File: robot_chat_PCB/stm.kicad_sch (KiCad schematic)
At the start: 12 parts, among them J3 Conn_02x07_Odd_Even, SW1 SW_Push, U1 STM32G070RBTx, Y1 16MHz

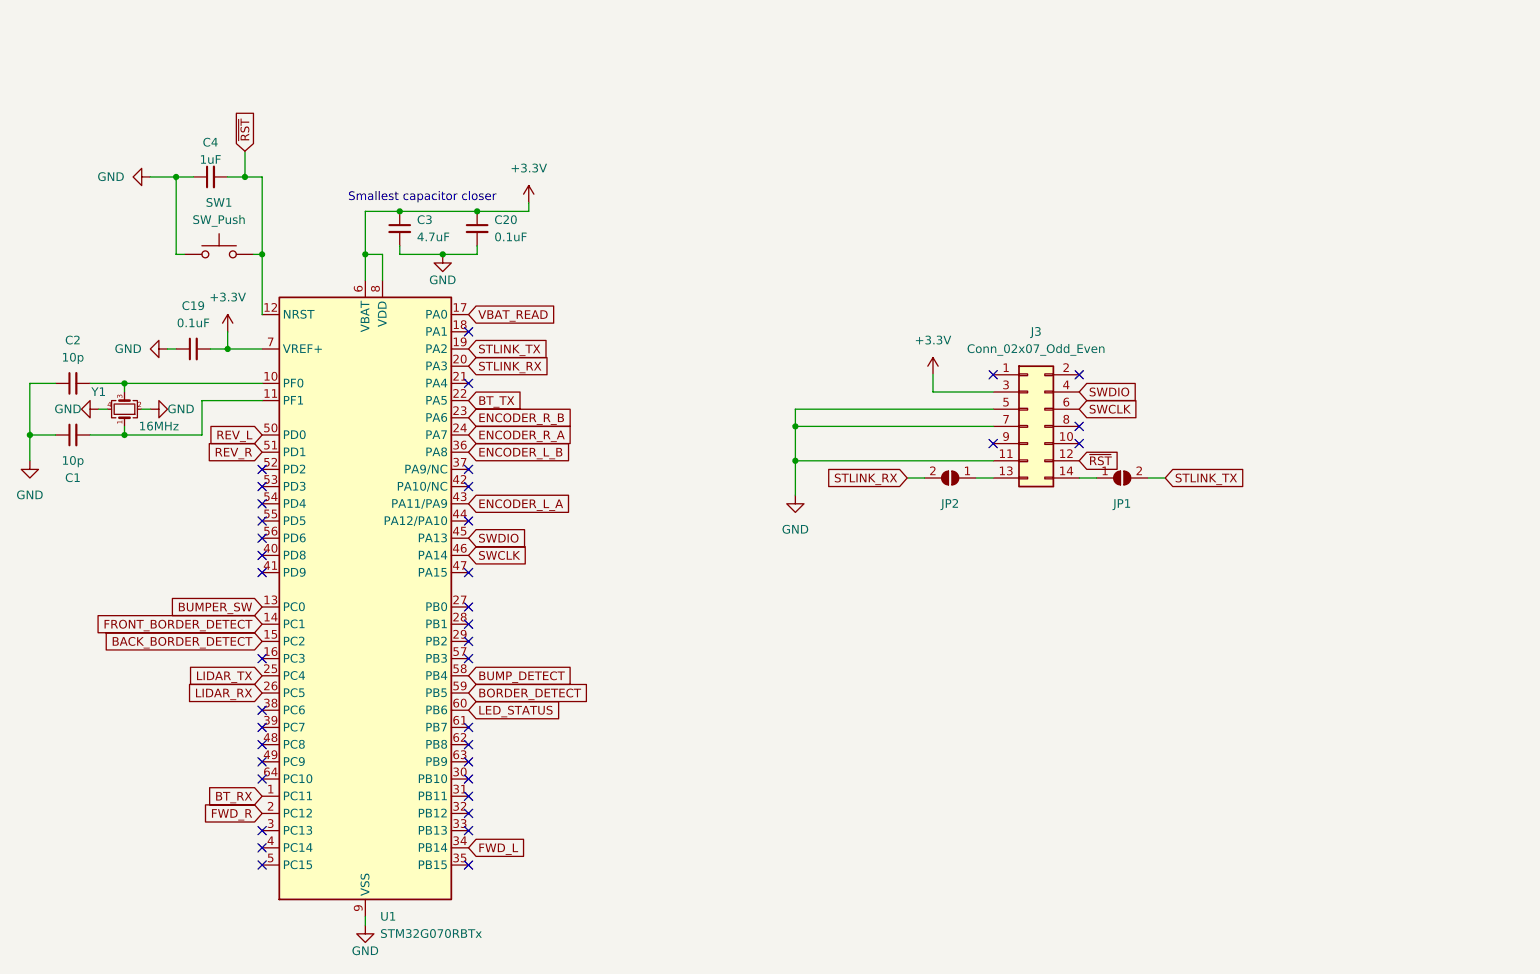
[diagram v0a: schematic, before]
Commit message: pcb alim et connecteurs
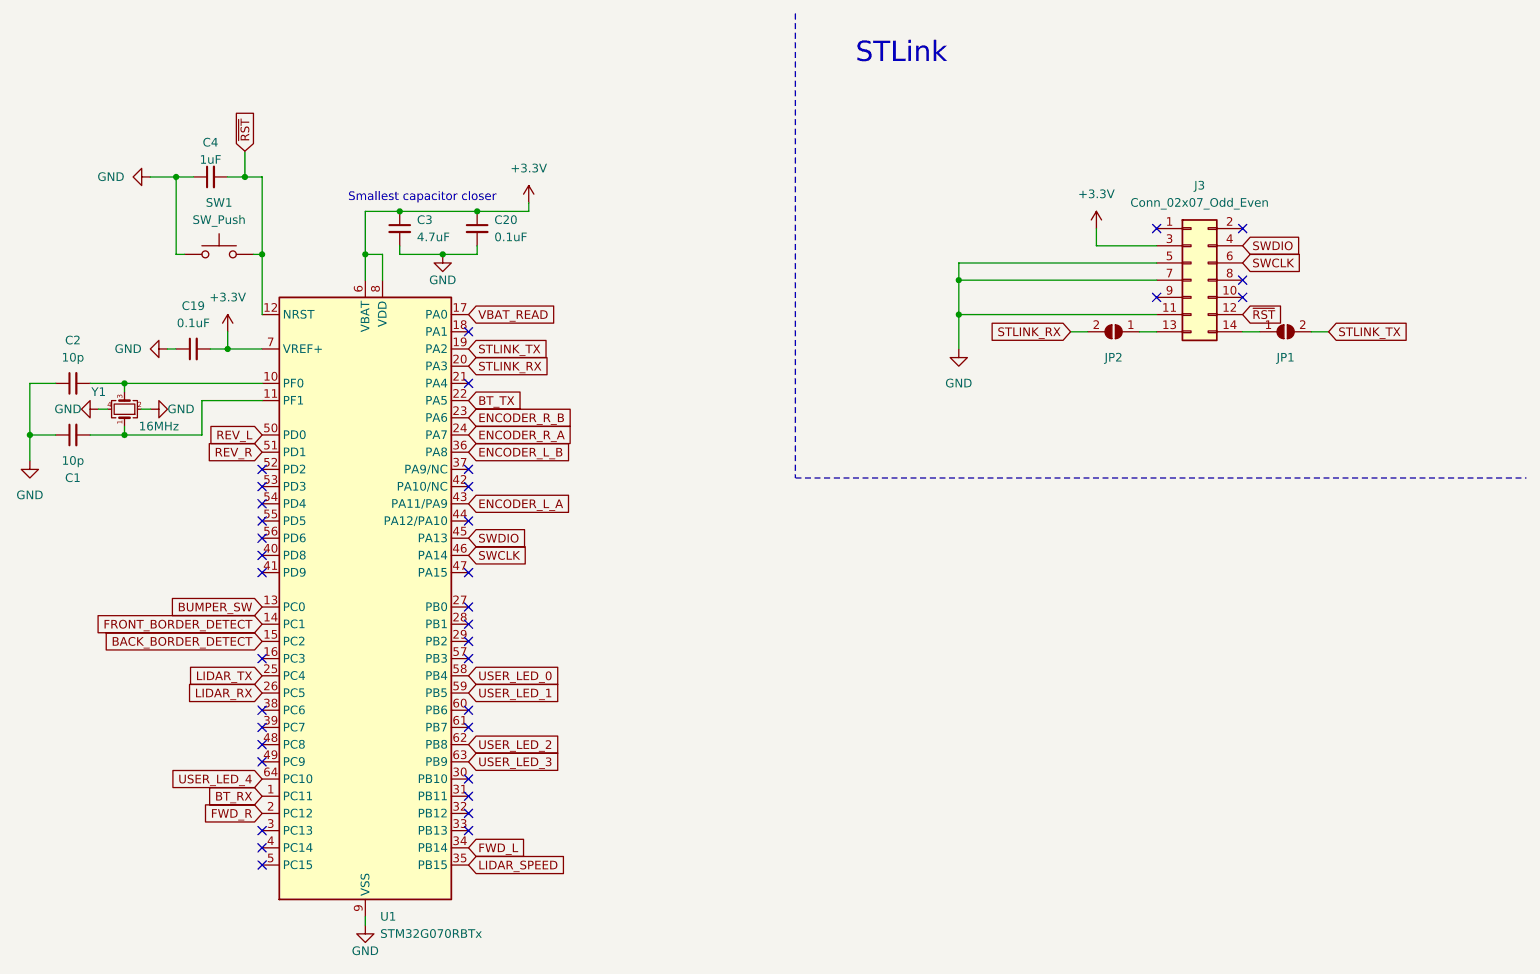
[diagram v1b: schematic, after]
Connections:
- net LIDAR_SPEED: now reaches U1.35 (PB15)
- net USER_LED_2: now reaches U1.62 (PB8)
- net USER_LED_3: now reaches U1.63 (PB9)
- net USER_LED_4: now reaches U1.64 (PC10)
- net BORDER_DETECT renamed USER_LED_1
- net BUMP_DETECT renamed USER_LED_0
- net LED_STATUS: no longer names the net of U1.60 (PB6)
- no-connect marks 39 -> 36
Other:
- note added: "STLink"
- moved on the sheet: J3, JP1, JP2
